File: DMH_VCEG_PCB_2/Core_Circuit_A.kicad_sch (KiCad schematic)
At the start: 104 parts, among them J21 Conn_01x10_PinHeader, J22 Conn_01x10_PinHeader, J24 Conn_01x06_PinHeader, Q1 BC558, Q10 BC548, Q2 BC558, Q3 BC548, Q4 BC548, Q5 MMBFJ113, Q6 MMBFJ113, Q7 BC548, Q8 BC548, Q9 BC548, SW1 SW_DPDT_x2_On-Off-(On), SW2 SW_DPDT_x2, SW3 SW_SPDT, U1 TL074, U2 4001, U22 CD4066BE, U3 40106, U4 CD4066BE, U5 TL074, U6 4001, U7 TL074

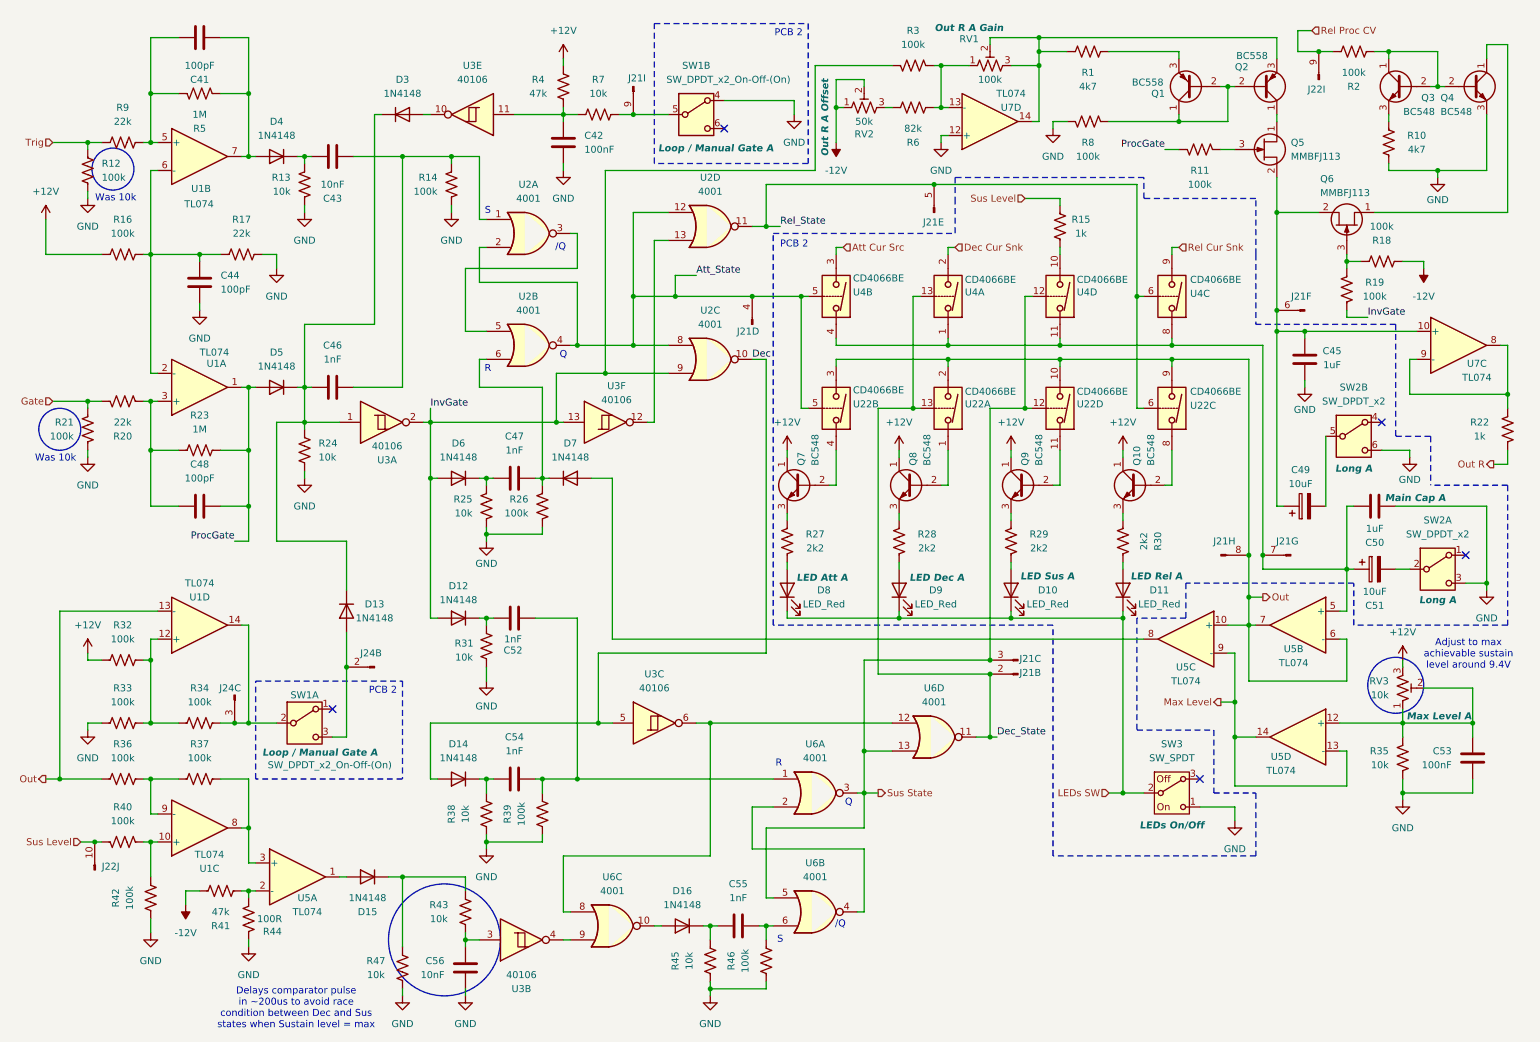
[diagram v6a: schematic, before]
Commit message: PCB 2 placement in progress
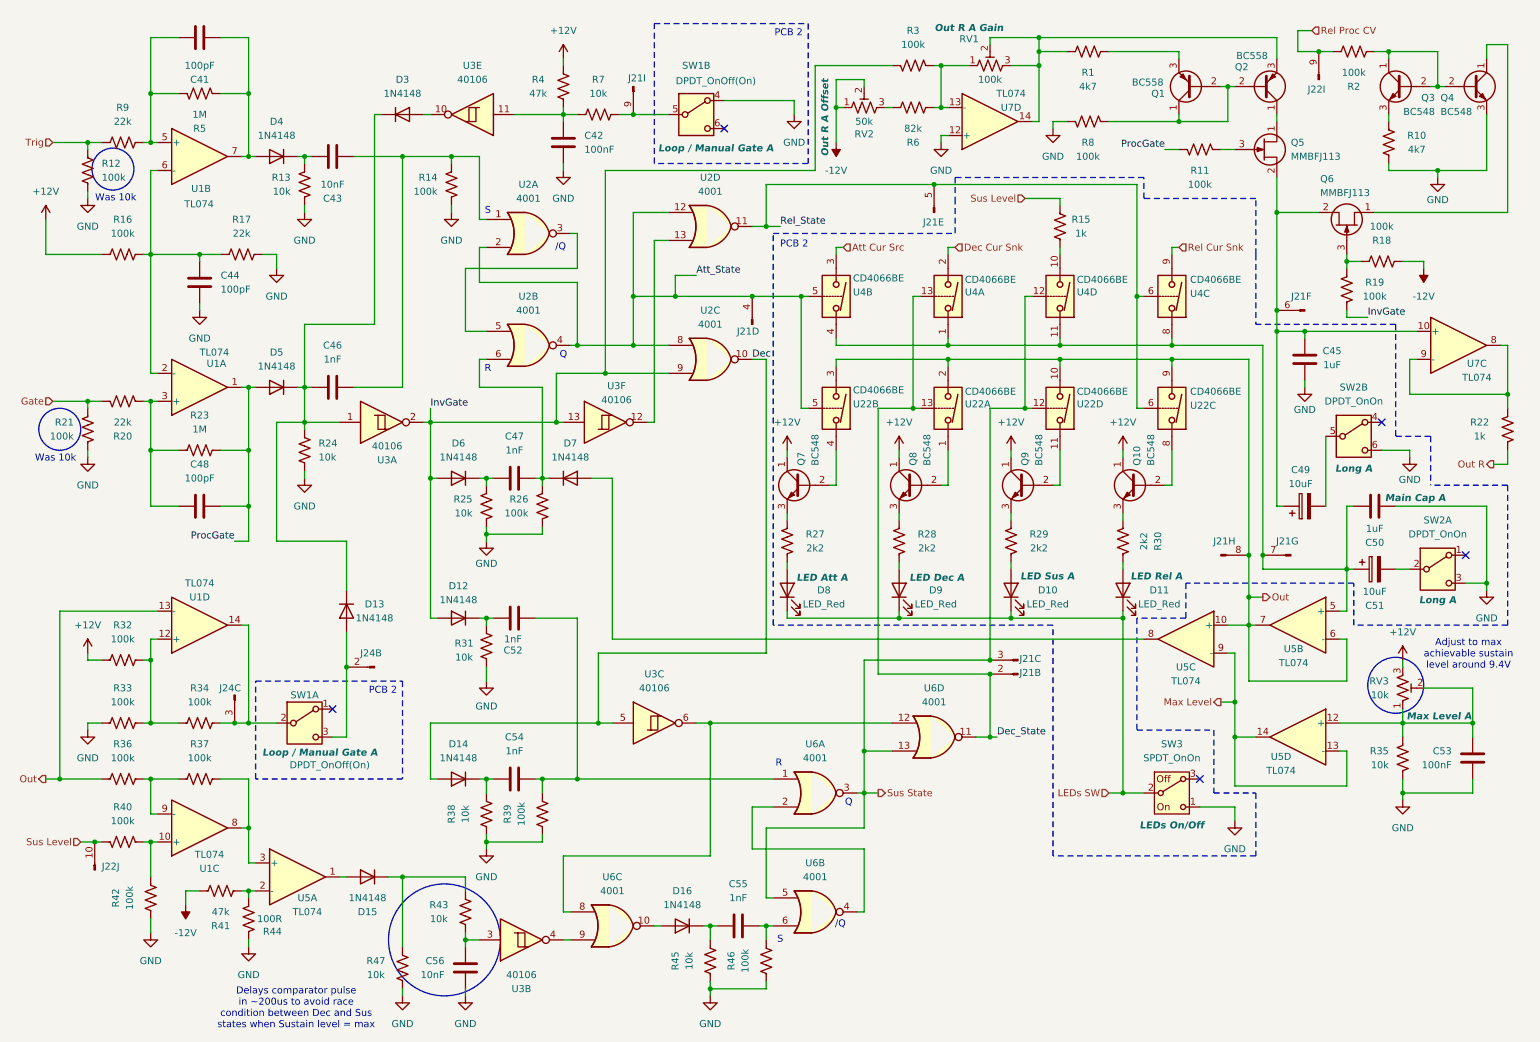
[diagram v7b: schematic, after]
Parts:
- SW1: value SW_DPDT_x2_On-Off-(On) -> DPDT_OnOff(On)
- SW2: value SW_DPDT_x2 -> DPDT_OnOn
- SW3: value SW_SPDT -> SPDT_OnOn
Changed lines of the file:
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@@
 			)
 		)
-		(property "Value" "SW_SPDT"
+		(property "Value" "SPDT_OnOn"
 			(at 222.25 147.32 0)
 			(effects
@@
 			)
 		)
-		(property "Value" "SW_DPDT_x2_On-Off-(On)"
-			(at 141.732 24.13 0)
+		(property "Value" "DPDT_OnOff(On)"
+			(at 139.446 24.384 0)
 			(effects
 				(font
@@
 			)
 		)
-		(property "Value" "SW_DPDT_x2"
+		(property "Value" "DPDT_OnOn"
 			(at 255.27 82.55 0)
 			(effects
@@
 			)
 		)
-		(property "Value" "SW_DPDT_x2_On-Off-(On)"
+		(property "Value" "DPDT_OnOff(On)"
 			(at 69.342 148.59 0)
 			(effects
@@
 			)
 		)
-		(property "Value" "SW_DPDT_x2"
+		(property "Value" "DPDT_OnOn"
 			(at 270.51 106.68 0)
 			(effects

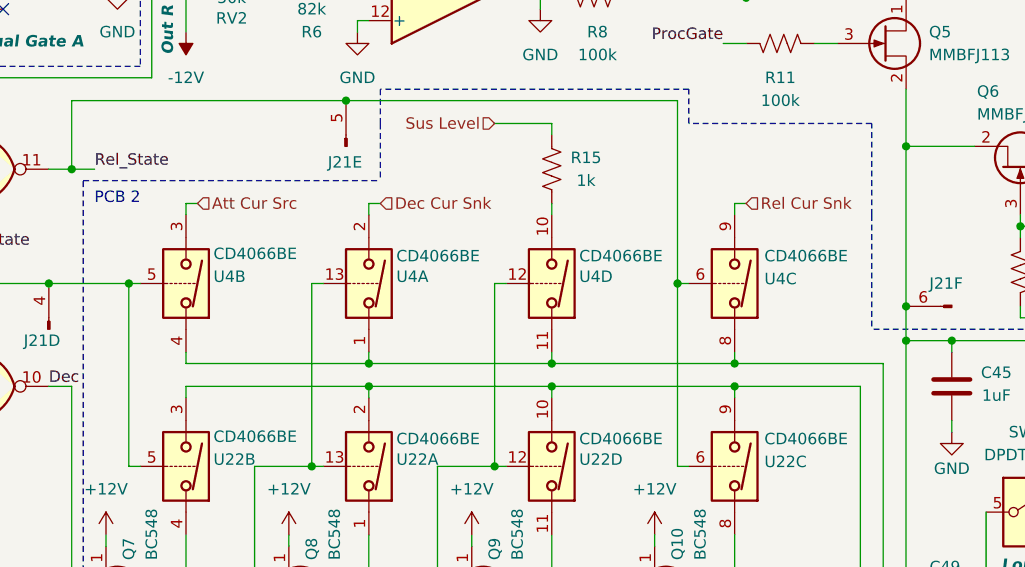
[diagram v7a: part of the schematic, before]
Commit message: Small changes during breadboarding
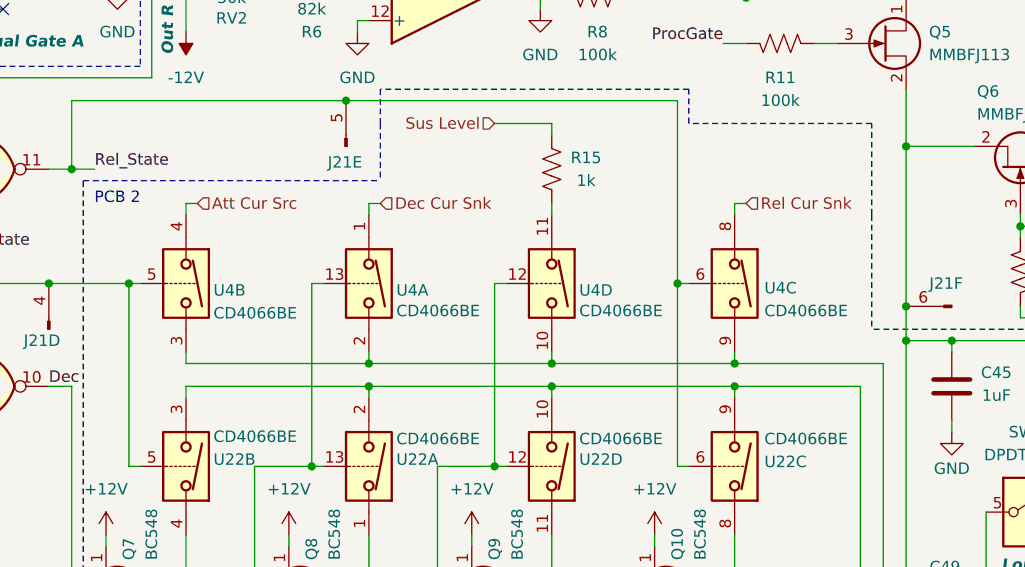
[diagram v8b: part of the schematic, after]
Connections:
- net Att Cur Src: now also U4.4; no longer U4.3
- net Dec Cur Snk: now also U4.1; no longer U4.2
- net Rel Cur Snk: now also U4.8; no longer U4.9
- net at C50.1, C51.1, J21.7 (Pin_7)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: now also U4.10, U4.2, U4.3, U4.9; no longer U4.1, U4.11, U4.4, U4.8
- net at R15.1: now also U4.11; no longer U4.10
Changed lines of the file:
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@@
 		(lib_id "Analog_Switch:CD4066BE")
 		(at 201.93 63.5 270)
-		(mirror x)
 		(unit 4)
 		(exclude_from_sim no)
@@
 		(dnp no)
 		(property "Reference" "U4"
-			(at 204.978 62.738 90)
+			(at 204.978 64.262 90)
 			(effects
 				(font
@@
 		)
 		(property "Value" "CD4066BE"
-			(at 204.978 60.452 90)
+			(at 204.978 66.548 90)
 			(effects
 				(font
@@
 		(lib_id "Analog_Switch:CD4066BE")
 		(at 181.61 63.5 270)
-		(mirror x)
 		(unit 1)
 		(exclude_from_sim no)
@@
 		(dnp no)
 		(property "Reference" "U4"
-			(at 184.658 62.738 90)
+			(at 184.658 64.262 90)
 			(effects
 				(font
@@
 		)
 		(property "Value" "CD4066BE"
-			(at 184.658 60.4521 90)
+			(at 184.658 66.5479 90)
 			(effects
 				(font
@@
 		(lib_id "Analog_Switch:CD4066BE")
 		(at 222.25 63.5 270)
-		(mirror x)
 		(unit 3)
 		(exclude_from_sim no)
@@
 		(dnp no)
 		(property "Reference" "U4"
-			(at 225.552 62.992 90)
+			(at 225.552 64.008 90)
 			(effects
 				(font
@@
 		)
 		(property "Value" "CD4066BE"
-			(at 225.552 60.452 90)
+			(at 225.552 66.548 90)
 			(effects
 				(font
@@
 		(lib_id "Analog_Switch:CD4066BE")
 		(at 161.29 63.5 270)
-		(mirror x)
 		(unit 2)
 		(exclude_from_sim no)
@@
 		(dnp no)
 		(property "Reference" "U4"
-			(at 164.338 62.738 90)
+			(at 164.338 64.262 90)
 			(effects
 				(font
@@
 		)
 		(property "Value" "CD4066BE"
-			(at 164.338 60.198 90)
+			(at 164.338 66.802 90)
 			(effects
 				(font
